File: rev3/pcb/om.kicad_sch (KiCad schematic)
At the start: 46 parts, among them J1 USB_C_Receptacle, J2 JST-BATT, J3 USB, J4 SWD, J5 USB, Q1 AO3407, Q2 AO3407, SW1 Choc, SW10 Choc, SW11 Choc, SW12 Choc, SW13 Choc, SW14 Choc, SW15 Choc, SW16 Choc, SW17 Choc, SW2 Choc, SW3 Choc, SW4 Choc, SW5 Choc, SW6 Choc, SW7 Choc, SW8 Choc, SW9 Choc, U1 nRF52840_holyiot_18010, U2 XC6206P LDO, U3 LTC4054ES5-4.2

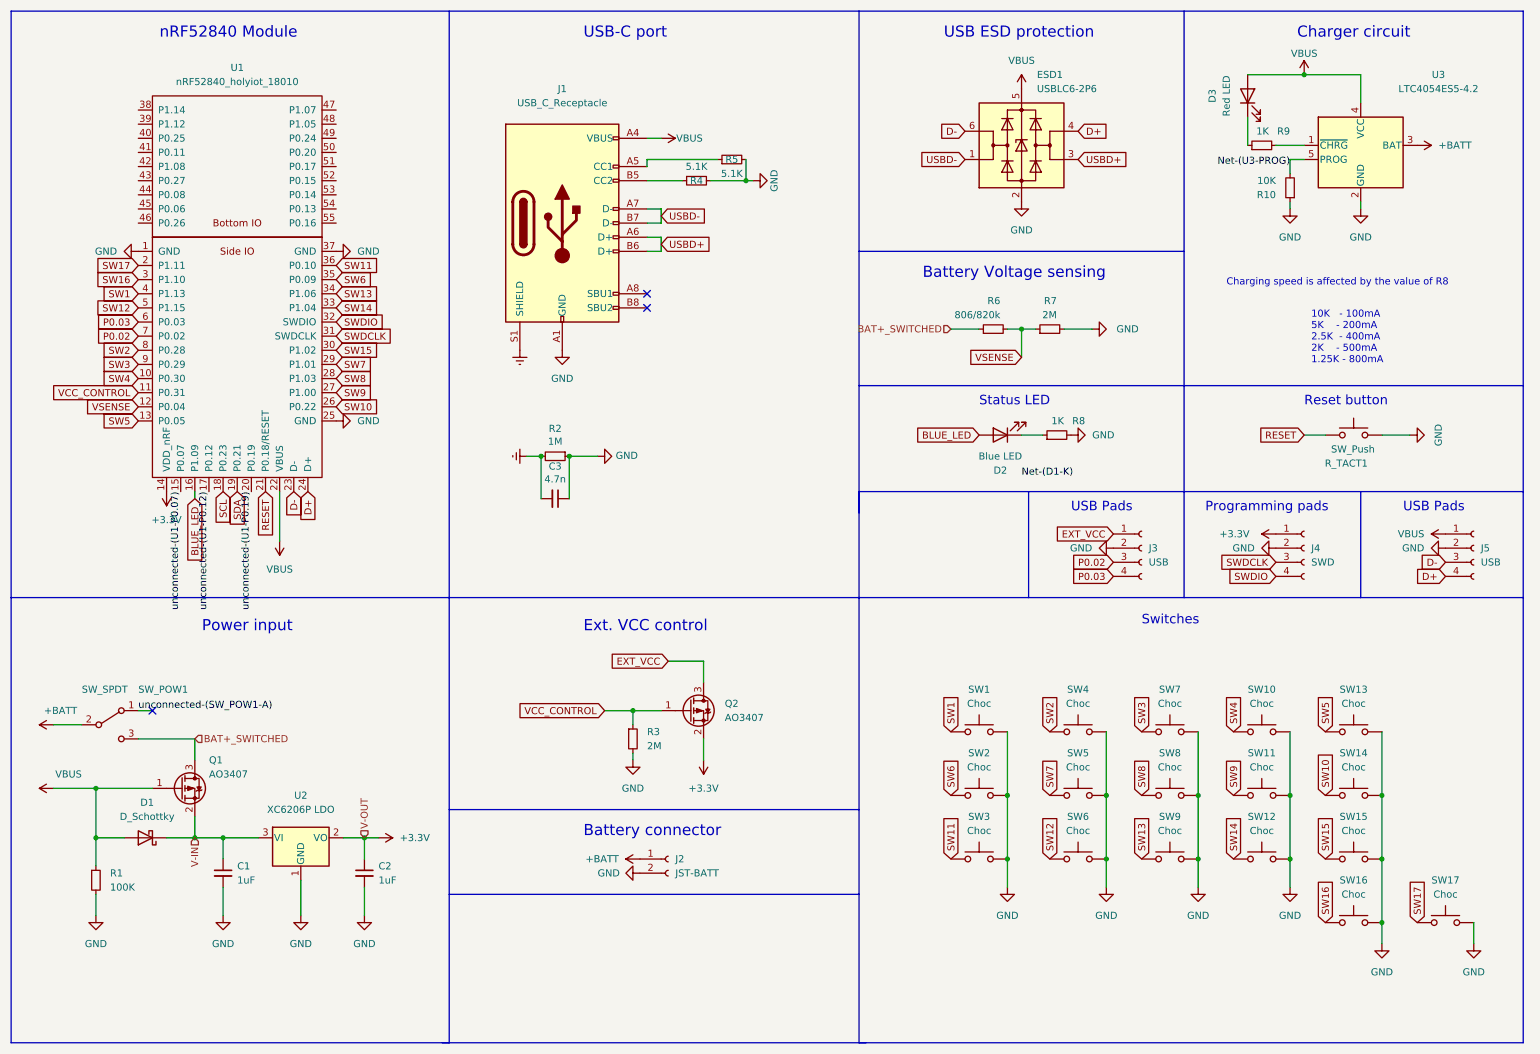
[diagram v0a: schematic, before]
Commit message: Fix up the schematic -> footprint library usage.  Pins were on the wrong pads.
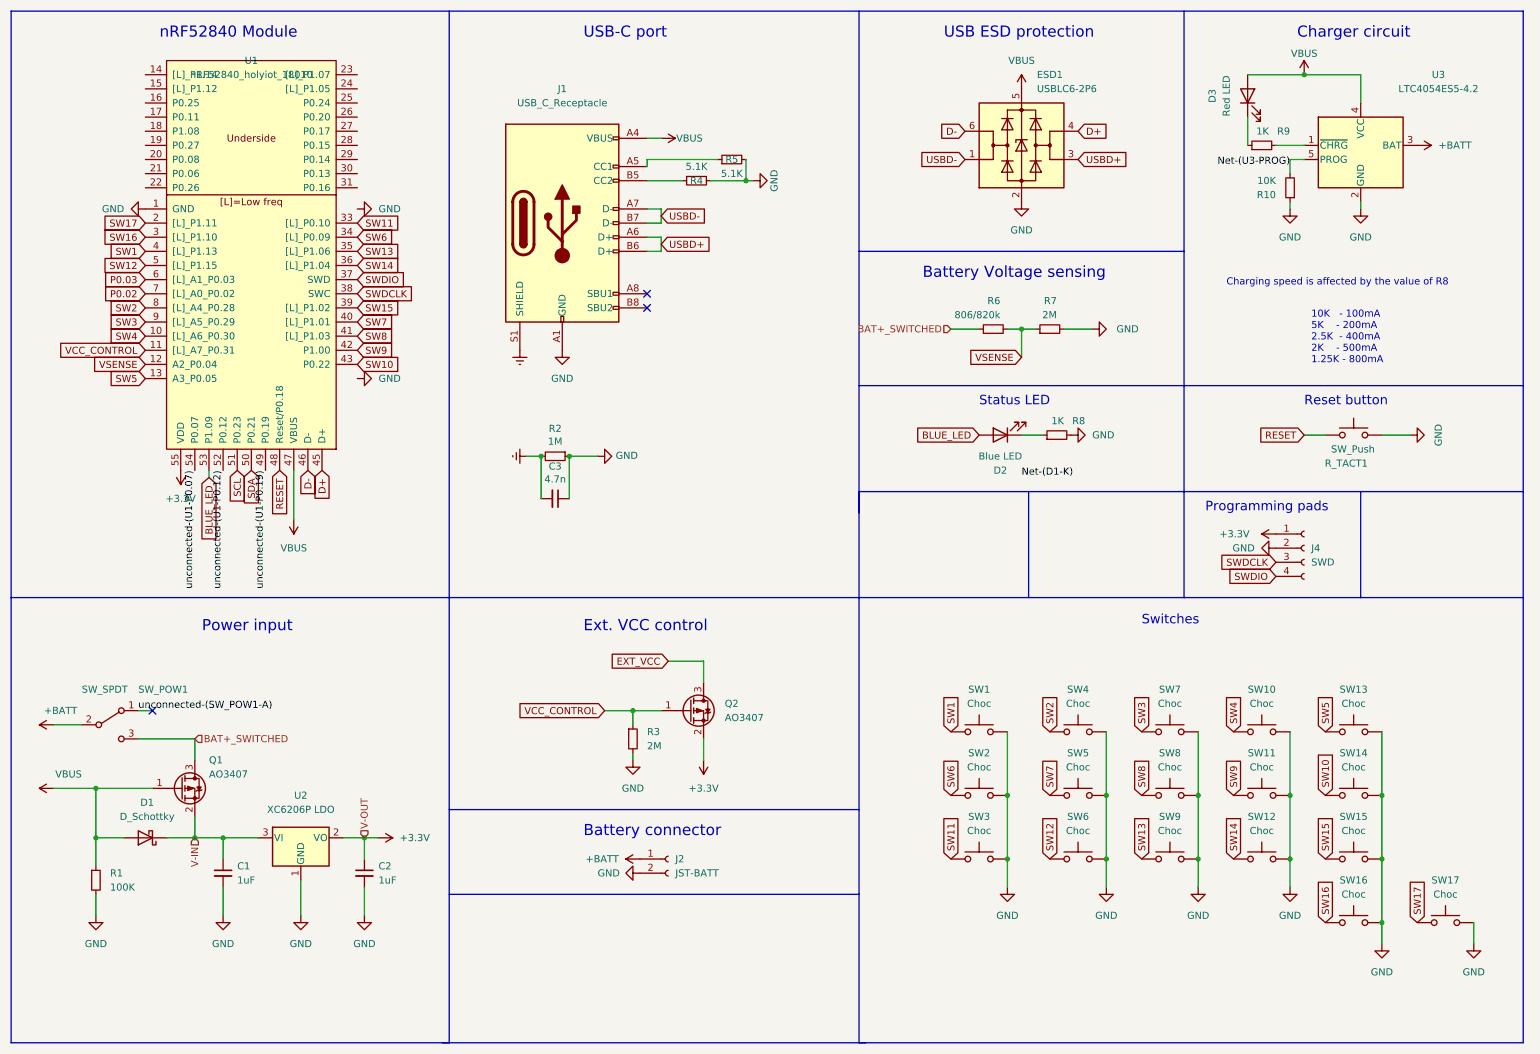
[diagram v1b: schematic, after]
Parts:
- removed J3: USB, Connector_PinHeader_2.00mm:PinHeader_1x04_P2.00mm_Vertical, symbol Connector:Conn_01x04_Female
- removed J5: USB, Connector_PinSocket_2.00mm:PinSocket_1x04_P2.00mm_Vertical, symbol Connector:Conn_01x04_Female
- U1: footprint kleeb-mcu:holyiot-18010 -> mcu:holyiot-18010; symbol kicad-keyboard-parts:nRF52840_holyiot_18010 -> kleeb-mcu:holyiot-18010
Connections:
- net +3V3: now also U1.55 (VDD); no longer U1.14 (VDD_nRF)
- net BLUE_LED: now also U1.53 (P1.09); no longer U1.16 (P1.09)
- net D+: now also U1.45 (D+); no longer U1.24 (D+)
- net D-: now also U1.46 (D-); no longer U1.23 (D-)
- net GND: now also U1.32 (GND), U1.44 (GND); no longer U1.25 (GND), U1.37 (GND)
- net RESET: now also U1.48 (Reset/P0.18); no longer U1.21 (P0.18/RESET)
- net SCL: now also U1.51 (P0.23); no longer U1.18 (P0.23)
- net SDA: now also U1.50 (P0.21); no longer U1.19 (P0.21)
- net SW10: now also U1.43 (P0.22); no longer U1.26 (P0.22)
- net SW11: now also U1.33 ([L]_P0.10); no longer U1.36 (P0.10)
- net SW13: now also U1.35 ([L]_P1.06); no longer U1.34 (P1.06)
- net SW14: now also U1.36 ([L]_P1.04); no longer U1.33 (P1.04)
- net SW15: now also U1.39 ([L]_P1.02); no longer U1.30 (P1.02)
- net SW6: now also U1.34 ([L]_P0.09); no longer U1.35 (P0.09)
- net SW7: now also U1.40 ([L]_P1.01); no longer U1.29 (P1.01)
- net SW8: now also U1.41 ([L]_P1.03); no longer U1.28 (P1.03)
- net SW9: now also U1.42 (P1.00); no longer U1.27 (P1.00)
- net SWDCLK: now also U1.38 (SWC); no longer U1.31 (SWDCLK)
- net SWDIO: now also U1.37 (SWD); no longer U1.32 (SWDIO)
- net VBUS: now also U1.47 (VBUS); no longer U1.22 (VBUS)
- net unconnected-(U1-P0.07): now also U1.54 (P0.07); no longer U1.15 (P0.07)
- net unconnected-(U1-P0.12): now also U1.52 (P0.12); no longer U1.17 (P0.12)
- net unconnected-(U1-P0.19): now also U1.49 (P0.19); no longer U1.20 (P0.19)
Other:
- note removed: "USB Pads"

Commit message: Routing might be done?
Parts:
- R_TACT1: footprint Button_Switch_SMD:SW_SPST_TL3342 -> om-footprints:SKHLLCA010
- SW1, SW10, SW11, SW12, SW13, SW14, SW15, SW16, SW17, SW2, SW3, SW4, SW5, SW6, SW7, SW8, SW9: footprint kleeb-pg1350:pg1350-R -> kleeb-pg1350:pg1350-DR; symbol Switch:SW_Push -> kleeb-switches:diode-choc
- U1: footprint mcu:holyiot-18010 -> kleeb-mcu:holyiot-18010
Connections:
- net GND: no longer SW1.2, SW10.2, SW11.2, SW12.2, SW13.2, SW14.2, SW15.2, SW16.2, SW17.2, SW2.2, SW3.2, SW4.2, SW5.2, SW6.2, SW7.2, SW8.2, SW9.2
- net SW1 renamed Col1
- net Col1: now also SW2.1, SW3.1, U1.2 ([L]_P1.11); no longer U1.4 ([L]_P1.13)
- net SW10: no longer names the net of U1.43 (P0.22)
- net SW10: no longer SW14.1
- net SW11: no longer names the net of U1.33 ([L]_P0.10)
- net SW11: no longer SW3.1
- net SW12 renamed Col2
- net Col2: now also SW4.1, SW5.1, U1.3 ([L]_P1.10); no longer U1.5 ([L]_P1.15)
- net SW13 renamed Col3
- net Col3: now also SW7.1, SW8.1, U1.4 ([L]_P1.13); no longer U1.35 ([L]_P1.06)
- net SW14 renamed Col4
- net Col4: now also SW10.1, SW11.1, SW16.1, U1.5 ([L]_P1.15); no longer U1.36 ([L]_P1.04)
- net SW15 renamed Col5
- net Col5: now also SW13.1, SW14.1, SW17.1, U1.41 ([L]_P1.03); no longer U1.39 ([L]_P1.02)
- removed net SW16: SW16.1, U1.3 ([L]_P1.10)
- removed net SW17: SW17.1, U1.2 ([L]_P1.11)
- net SW2: no longer names the net of U1.8 ([L]_A4_P0.28)
- net SW2: no longer SW4.1
- net SW3: no longer names the net of U1.9 ([L]_A5_P0.29)
- net SW3: no longer SW7.1
- net SW4: no longer names the net of U1.10 ([L]_A6_P0.30)
- net SW4: no longer SW10.1
- net SW5: no longer names the net of U1.13 (A3_P0.05)
- net SW5: no longer SW13.1
- net SW6: no longer names the net of U1.34 ([L]_P0.09)
- net SW6: no longer SW2.1
- net SW7 renamed Row1
- net Row1: now also SW1.2, SW10.2, SW13.2, SW4.2, SW7.2; no longer SW5.1
- removed net SW8: SW8.1, U1.41 ([L]_P1.03)
- net SW9: no longer names the net of U1.42 (P1.00)
- net SW9: no longer SW11.1
- net unconnected-(U1-P0.07): no longer names the net of U1.54 (P0.07)
- net unconnected-(U1-P0.12): no longer names the net of U1.52 (P0.12)
- net unconnected-(U1-P0.19): no longer names the net of U1.49 (P0.19)
- new net Row2: SW11.2, SW14.2, SW2.2, SW5.2, SW8.2, U1.39 ([L]_P1.02)
- new net Row3: SW12.2, SW15.2, SW3.2, SW6.2, SW9.2, U1.36 ([L]_P1.04)
- new net Row4: SW16.2, SW17.2, U1.35 ([L]_P1.06)
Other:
- moved on the sheet: J4, U1

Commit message: Mostly in place, time to refactor
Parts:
- added DIODE1, DIODE10, DIODE11, DIODE12, DIODE13, DIODE14, DIODE15, DIODE16, DIODE17, DIODE2, DIODE3, DIODE4, DIODE5, DIODE6, DIODE7, DIODE8, DIODE9: 1N914WT, Diode_SMD:D_SOD-123, symbol Diode:1N914WT
- added J3: JST-BATT, Connector_JST:JST_PH_S2B-PH-K_1x02_P2.00mm_Horizontal, symbol Connector:Conn_01x02_Female
- C1, C2: LCSC (none) -> C15849
- C3: LCSC (none) -> C1744
- D1: LCSC (none) -> C191023
- R_TACT1: LCSC (none) -> C139766
- SW1, SW10, SW11, SW12, SW13, SW14, SW15, SW16, SW17, SW2, SW3, SW4, SW5, SW6, SW7, SW8, SW9: footprint kleeb-pg1350:pg1350-DR -> kleeb-pg1350:pg1350; symbol kleeb-switches:diode-choc -> Switch:SW_Push
- U3: LCSC (none) -> C462648
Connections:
- net +BATT: now also J3.1 (Pin_1)
- net GND: now also J3.2 (Pin_2); no longer R7.2
- net Row1: now also DIODE1.1 (K), DIODE10.1 (K), DIODE13.1 (K), DIODE4.1 (K), DIODE7.1 (K); no longer SW1.2, SW10.2, SW13.2, SW4.2, SW7.2
- net Row2: now also DIODE11.1 (K), DIODE14.1 (K), DIODE2.1 (K), DIODE5.1 (K), DIODE8.1 (K); no longer SW11.2, SW14.2, SW2.2, SW5.2, SW8.2
- net Row3: now also DIODE12.1 (K), DIODE15.1 (K), DIODE3.1 (K), DIODE6.1 (K), DIODE9.1 (K); no longer SW12.2, SW15.2, SW3.2, SW6.2, SW9.2
- net Row4: now also DIODE16.1 (K), DIODE17.1 (K); no longer SW16.2, SW17.2
- net VSENSE_ENABLE: now reaches U1.10 ([L]_A6_P0.30)
- net VSENSE_ENABLE: now also R7.2
- net P0.02: no longer names the net of U1.7 ([L]_A0_P0.02)
- net P0.03: no longer names the net of U1.6 ([L]_A1_P0.03)
- new net: DIODE9.2 (A), SW9.2
- new net: DIODE4.2 (A), SW4.2
- new net: DIODE5.2 (A), SW5.2
- new net: DIODE15.2 (A), SW15.2
- new net: DIODE13.2 (A), SW13.2
- new net: DIODE16.2 (A), SW16.2
- new net: DIODE1.2 (A), SW1.2
- new net: DIODE17.2 (A), SW17.2
- new net: DIODE3.2 (A), SW3.2
- new net: DIODE2.2 (A), SW2.2
- new net: DIODE7.2 (A), SW7.2
- new net: DIODE11.2 (A), SW11.2
- new net: DIODE12.2 (A), SW12.2
- new net: DIODE8.2 (A), SW8.2
- new net: DIODE6.2 (A), SW6.2
- new net: DIODE14.2 (A), SW14.2
- new net: DIODE10.2 (A), SW10.2
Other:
- moved on the sheet: J2, R6, R7
